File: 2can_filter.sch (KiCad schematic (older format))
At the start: 16 parts, among them J3 USB mini-B SMD, J4 NOT_FITTED_SWD_Conn_01x04_Male, U5 STM32F105RBTx, U6 TJA1040T, U7 TJA1040T, Y1 Crystal KX-13 25MHz

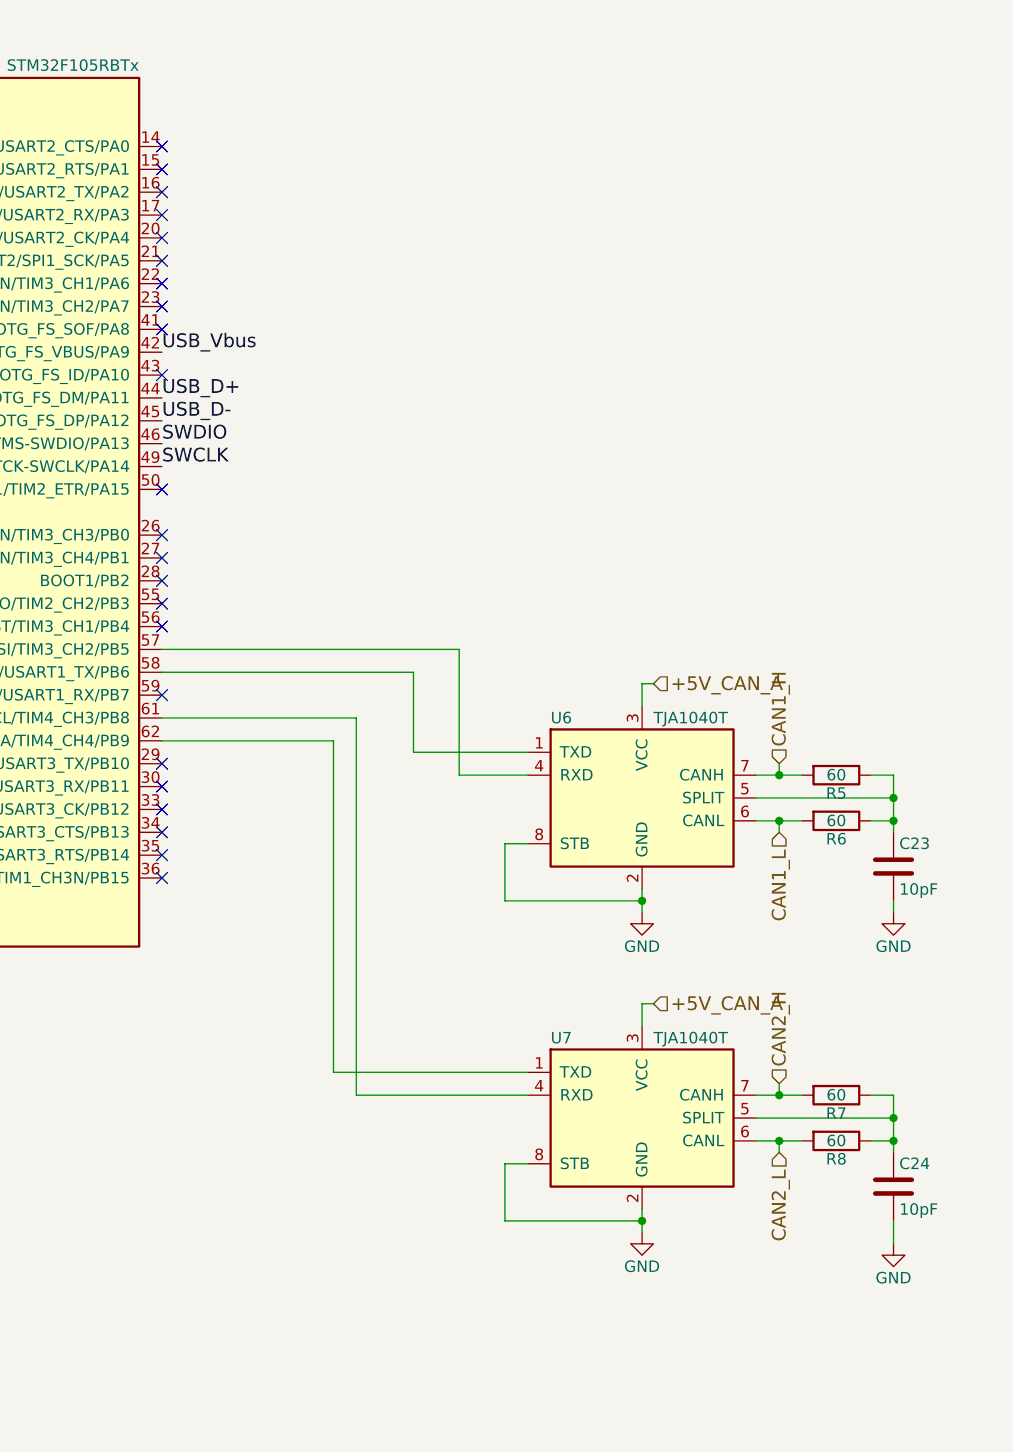
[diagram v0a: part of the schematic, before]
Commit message: add transient voltage suppression diods on CAN
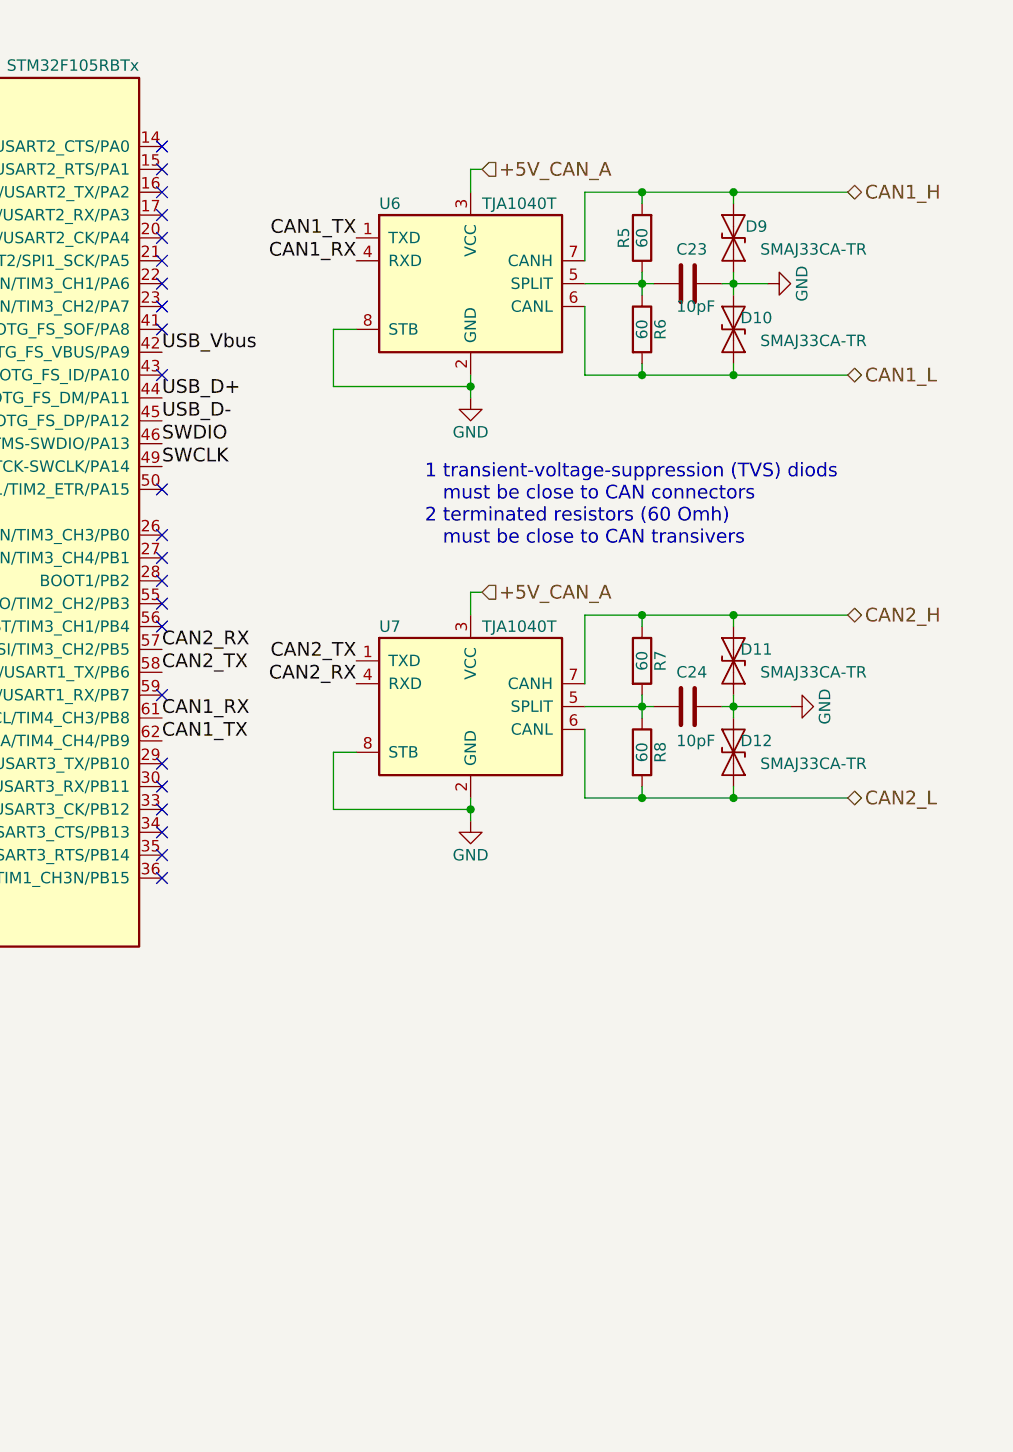
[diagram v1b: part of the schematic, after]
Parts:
- added D10, D11, D12, D9: SMAJ33CA-TR, Diodes_SMD:D_SMA, symbol D_TVS
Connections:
- net CAN1_H: now also D9.1 (A1)
- net CAN1_L: now also D10.2 (A2)
- net CAN2_H: now also R7.1, D11.1 (A1); no longer R7.2
- net CAN2_L: now also D12.2 (A2)
- net GND: now also C23.1, C24.1, D10.1 (A1), D11.2 (A2), D12.1 (A1), D9.2 (A2); no longer C23.2, C24.2
- net CAN1_TX: now reaches U5.62 (CAN1_TX/DAC_EXTI9/I2C1_SDA/TIM4_CH4/PB9)
- net CAN1_TX: now also U6.1 (TXD); no longer U7.1 (TXD)
- net CAN1_RX: now reaches U5.61 (CAN1_RX/I2C1_SCL/TIM4_CH3/PB8)
- net CAN1_RX: now also U6.4 (RXD); no longer U7.4 (RXD)
- net at R8.1, U7.5 (SPLIT): now also C24.2, R7.2; no longer C24.1, R7.1
- net CAN2_RX: now reaches U5.57 (CAN2_RX/I2C1_SMBA/I2S3_SD/SPI1_MOSI/SPI3_MOSI/TIM3_CH2/PB5)
- net CAN2_RX: now also U7.4 (RXD); no longer U6.4 (RXD)
- net CAN2_TX: now reaches U5.58 (CAN2_TX/I2C1_SCL/TIM4_CH1/USART1_TX/PB6)
- net CAN2_TX: now also U7.1 (TXD); no longer U6.1 (TXD)
- net at R5.1, R6.1, U6.5 (SPLIT): now also C23.2; no longer C23.1
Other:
- note added: "1 transient-voltage-suppression (TVS) diods\n must be close to CAN connectors\n2 terminated resistors (60 Omh)\n must be close to CAN transivers"
- moved on the sheet: C23, C24, R5, R6, R7, R8, U6, U7

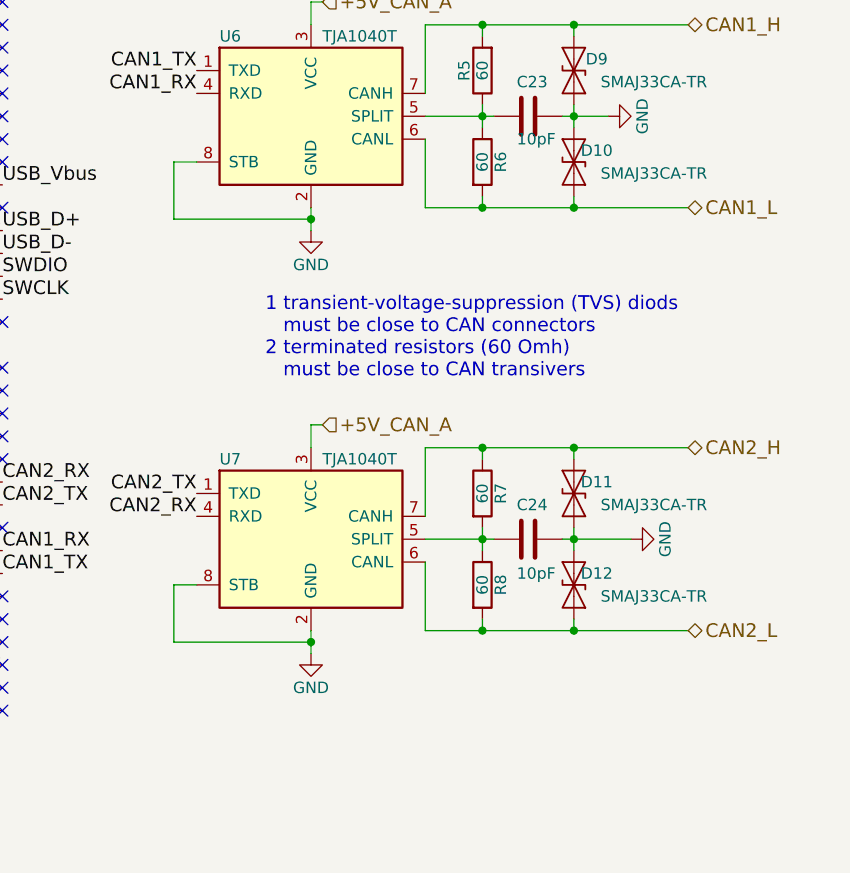
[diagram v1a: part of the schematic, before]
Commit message: add resistor on can STB pin module A
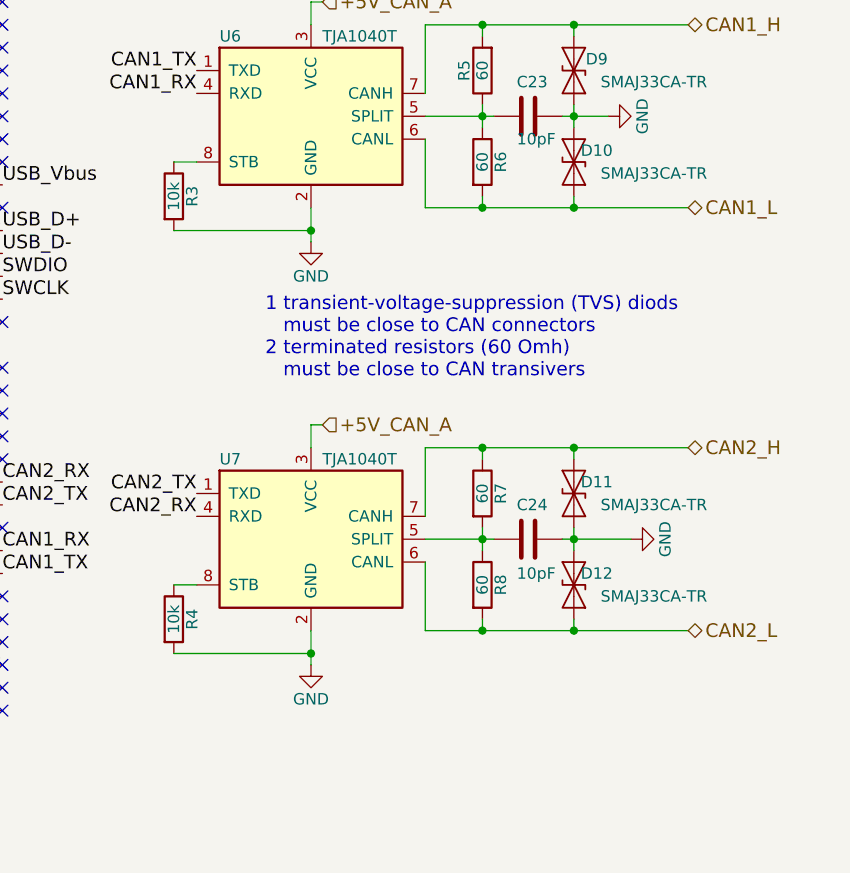
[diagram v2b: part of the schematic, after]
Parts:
- added R3, R4: 10k, Resistors_SMD:R_0805, symbol R
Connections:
- net GND: now also R3.2, R4.2; no longer U6.8 (STB), U7.8 (STB)
- new net: R4.1, U7.8 (STB)
- new net: R3.1, U6.8 (STB)
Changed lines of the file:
@@
 L GND #PWR08
 U 1 1 5A048D0B
-P 9050 2400
-F 0 "#PWR08" H 9050 2150 50  0001 C CNN
-F 1 "GND" H 9050 2250 50  0000 C CNN
-F 2 "" H 9050 2400 50  0001 C CNN
-F 3 "" H 9050 2400 50  0001 C CNN
-	1    9050 2400
+P 9050 2450
+F 0 "#PWR08" H 9050 2200 50  0001 C CNN
+F 1 "GND" H 9050 2300 50  0000 C CNN
+F 2 "" H 9050 2450 50  0001 C CNN
+F 3 "" H 9050 2450 50  0001 C CNN
+	1    9050 2450
 	1    0    0    -1
 $EndComp
@@
 L GND #PWR09
 U 1 1 5A09EB28
-P 9050 4250
-F 0 "#PWR09" H 9050 4000 50  0001 C CNN
-F 1 "GND" H 9050 4100 50  0000 C CNN
-F 2 "" H 9050 4250 50  0001 C CNN
-F 3 "" H 9050 4250 50  0001 C CNN
-	1    9050 4250
+P 9050 4300
+F 0 "#PWR09" H 9050 4050 50  0001 C CNN
+F 1 "GND" H 9050 4150 50  0000 C CNN
+F 2 "" H 9050 4300 50  0001 C CNN
+F 3 "" H 9050 4300 50  0001 C CNN
+	1    9050 4300
 	1    0    0    -1
 $EndComp
@@
 	9050 1500 9050 1400
 Wire Wire Line
-	8450 2100 8450 2350
-Wire Wire Line
 	8450 2100 8550 2100
 Wire Wire Line
-	9050 2300 9050 2400
+	9050 2300 9050 2450
 Wire Wire Line
 	8450 3950 8550 3950
 Wire Wire Line
-	9050 4150 9050 4250
+	9050 4150 9050 4300
 Wire Wire Line
 	2100 6800 2100 6650
@@
 Connection ~ 5600 6600
 Wire Wire Line
-	8450 2350 9050 2350
-Connection ~ 9050 2350
-Wire Wire Line
-	9050 4200 8450 4200
-Connection ~ 9050 4200
-Wire Wire Line
-	8450 4200 8450 3950
+	8450 2400 9050 2400
+Connection ~ 9050 2400
+Wire Wire Line
+	9050 4250 8450 4250
+Connection ~ 9050 4250
 Wire Wire Line
 	9050 3350 9050 3250
@@
 	9550 4150 10700 4150
 Wire Wire Line
-	10700 3350 9550 3350
+	9550 3350 10700 3350
 Wire Wire Line
 	9550 3350 9550 3650
@@
 Text Notes 8850 3050 0    60   ~ 0
 1 transient-voltage-suppression (TVS) diods\n   must be close to CAN connectors\n2 terminated resistors (60 Omh)\n   must be close to CAN transivers
+$Comp
+L R R3
+U 1 1 5A16A204
+P 8450 2250
+F 0 "R3" V 8530 2250 50  0000 C CNN
+F 1 "10k" V 8450 2250 50  0000 C CNN
+F 2 "Resistors_SMD:R_0805" V 8380 2250 50  0001 C CNN
+F 3 "" H 8450 2250 50  0001 C CNN
+	1    8450 2250
+	1    0    0    -1
+$EndComp
+$Comp
+L R R4
+U 1 1 5A16A369
+P 8450 4100
+F 0 "R4" V 8530 4100 50  0000 C CNN
+F 1 "10k" V 8450 4100 50  0000 C CNN
+F 2 "Resistors_SMD:R_0805" V 8380 4100 50  0001 C CNN
+F 3 "" H 8450 4100 50  0001 C CNN
+	1    8450 4100
+	1    0    0    -1
+$EndComp
 $EndSCHEMATC

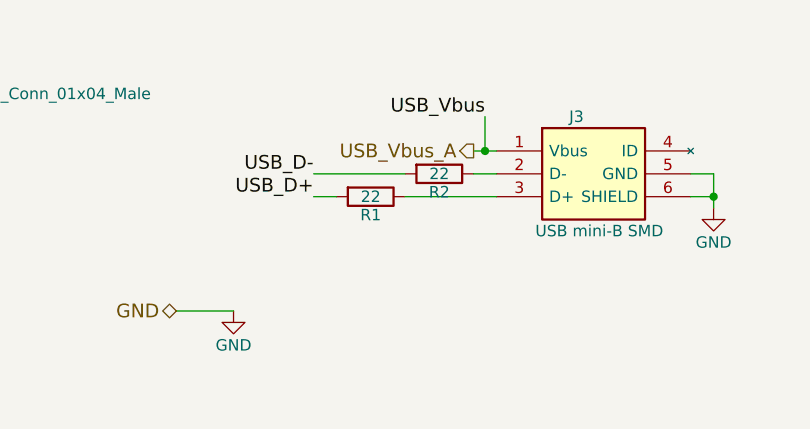
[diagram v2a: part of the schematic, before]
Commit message: fix signal trace length usb module A
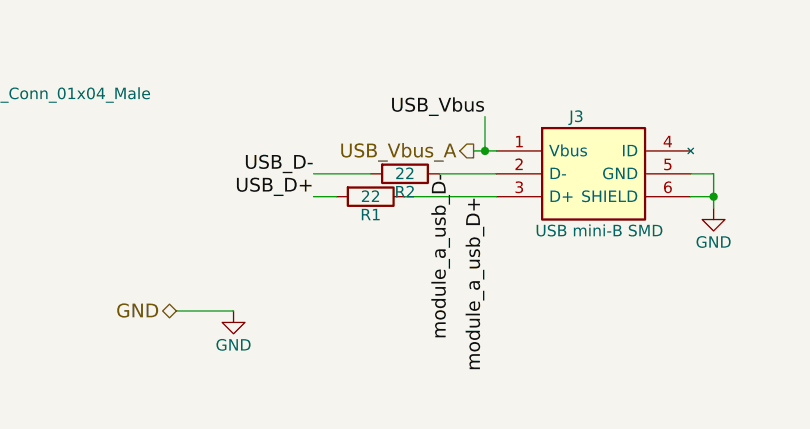
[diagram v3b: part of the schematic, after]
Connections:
- net module_a_usb_D-: now reaches J3.2 (D-), R2.1
- net module_a_usb_D+: now reaches J3.3 (D+), R1.1
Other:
- moved on the sheet: R2
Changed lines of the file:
@@
 L R R2
 U 1 1 5A0C2815
-P 4400 6500
-F 0 "R2" V 4480 6500 50  0000 C CNN
-F 1 "22" V 4400 6500 50  0000 C CNN
-F 2 "Resistors_SMD:R_0805" V 4330 6500 50  0001 C CNN
-F 3 "" H 4400 6500 50  0001 C CNN
-	1    4400 6500
+P 4250 6500
+F 0 "R2" V 4330 6500 50  0000 C CNN
+F 1 "22" V 4250 6500 50  0000 C CNN
+F 2 "Resistors_SMD:R_0805" V 4180 6500 50  0001 C CNN
+F 3 "" H 4250 6500 50  0001 C CNN
+	1    4250 6500
 	0    1    1    0
 $EndComp
@@
 	5600 6500 5600 6650
 Wire Wire Line
-	3850 6500 4250 6500
-Wire Wire Line
-	4550 6500 4650 6500
+	3850 6500 4100 6500
+Wire Wire Line
+	4400 6500 4650 6500
 Wire Wire Line
 	4650 6600 4250 6600
@@
 	1    0    0    -1
 $EndComp
+Text Label 4600 6600 3    60   ~ 0
+module_a_usb_D+
+Text Label 4450 6500 3    60   ~ 0
+module_a_usb_D-
 $EndSCHEMATC

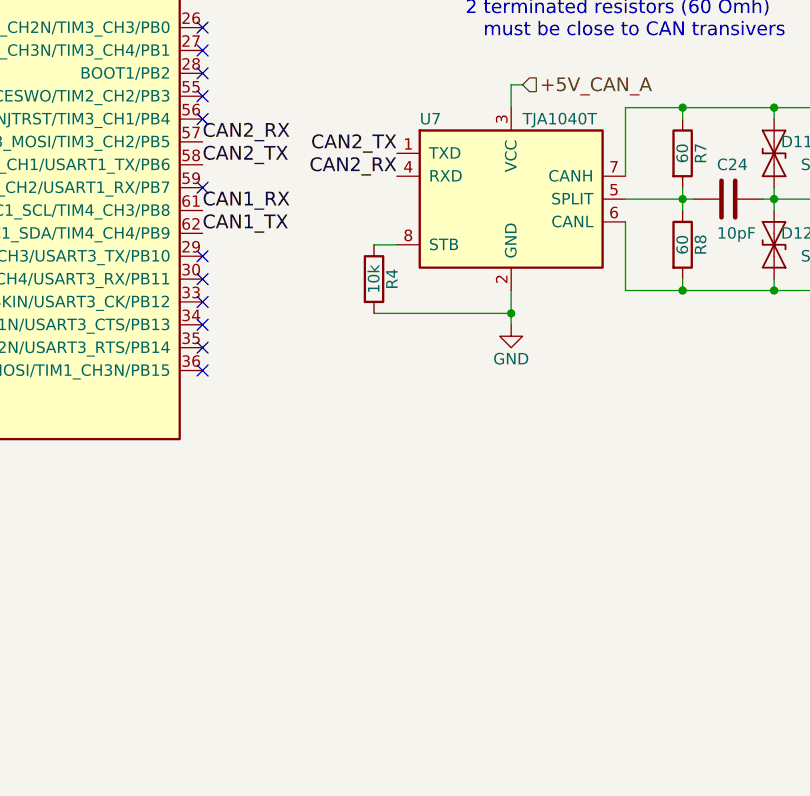
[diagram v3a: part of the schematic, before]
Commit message: sch&pcb: add LED`s and refresh readme image`s
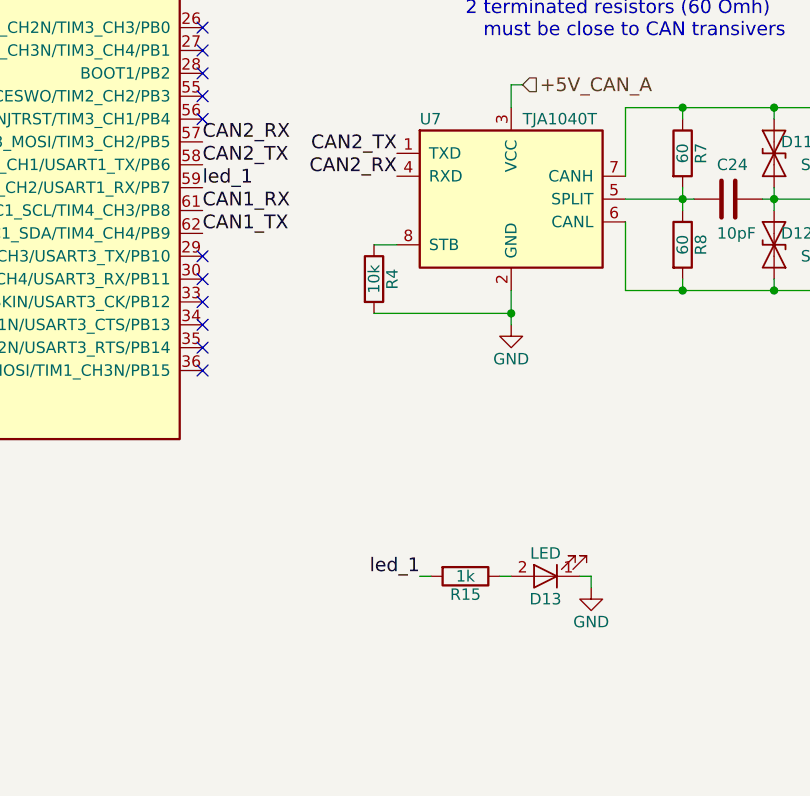
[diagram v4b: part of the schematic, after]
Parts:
- added D13: LED, LEDs:LED_0805, symbol LED
- added R15: 1k, Resistors_SMD:R_0805, symbol R
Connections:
- net GND: now also D13.1 (K)
- net led_1: now reaches U5.59 (I2C1_SDA/TIM4_CH2/USART1_RX/PB7)
- net led_1: now also R15.2
- new net: D13.2 (A), R15.1
- no-connect marks 42 -> 41
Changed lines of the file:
@@
 NoConn ~ 7700 4100
 NoConn ~ 7700 4000
-NoConn ~ 7700 3700
 NoConn ~ 7700 3400
 NoConn ~ 7700 3300
@@
 Text Label 4450 6500 3    60   ~ 0
 module_a_usb_D-
+$Comp
+L R R15
+U 1 1 5A2685DD
+P 8850 5400
+F 0 "R15" V 8930 5400 50  0000 C CNN
+F 1 "1k" V 8850 5400 50  0000 C CNN
+F 2 "Resistors_SMD:R_0805" V 8780 5400 50  0001 C CNN
+F 3 "" H 8850 5400 50  0001 C CNN
+	1    8850 5400
+	0    1    1    0
+$EndComp
+$Comp
+L LED D13
+U 1 1 5A26884C
+P 9200 5400
+F 0 "D13" H 9200 5500 50  0000 C CNN
+F 1 "LED" H 9200 5300 50  0000 C CNN
+F 2 "LEDs:LED_0805" H 9200 5400 50  0001 C CNN
+F 3 "" H 9200 5400 50  0001 C CNN
+	1    9200 5400
+	-1   0    0    1
+$EndComp
+Wire Wire Line
+	9000 5400 9050 5400
+Wire Wire Line
+	9350 5400 9400 5400
+Wire Wire Line
+	9400 5400 9400 5450
+Wire Wire Line
+	8700 5400 8650 5400
+$Comp
+L GND #PWR016
+U 1 1 5A268B13
+P 9400 5450
+F 0 "#PWR016" H 9400 5200 50  0001 C CNN
+F 1 "GND" H 9400 5300 50  0000 C CNN
+F 2 "" H 9400 5450 50  0001 C CNN
+F 3 "" H 9400 5450 50  0001 C CNN
+	1    9400 5450
+	1    0    0    -1
+$EndComp
+Text Label 8650 5400 2    60   ~ 0
+led_1
+Text Label 7700 3700 0    60   ~ 0
+led_1
 $EndSCHEMATC

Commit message: add usb 3d modele
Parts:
- J3: footprint zulljon:USB_mini_B -> zpkl:USB_mini_B
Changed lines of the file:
@@
 F 0 "J3" H 5000 6550 50  0000 C CNN
 F 1 "USB mini-B SMD" H 5100 6050 50  0000 C CNN
-F 2 "zulljon:USB_mini_B" H 5000 5950 50  0001 C CNN
+F 2 "zpkl:USB_mini_B" H 5000 5950 50  0001 C CNN
 F 3 "http://www.molex.com/webdocs/datasheets/pdf/en-us/0548190572_IO_CONNECTORS.pdf" H 5000 5850 50  0001 C CNN
 F 4 "Surface mount onthego connector,1A 30V Molex On-The-Go Series Right Angle SMT Version 2.0 Type B Mini USB Connector Receptacle, 30 V, 1A" H 5000 5750 50  0001 C CNN "Description"

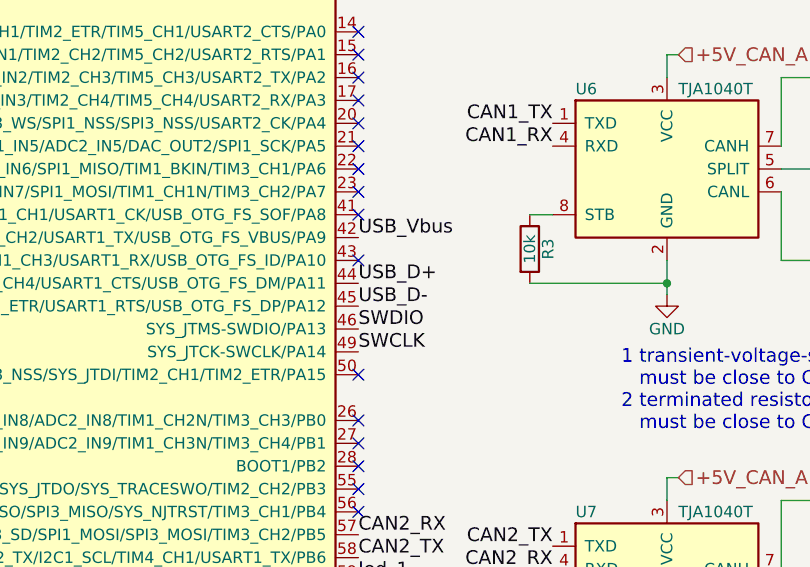
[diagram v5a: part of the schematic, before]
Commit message: fix USB, swapped the traces D+ D-
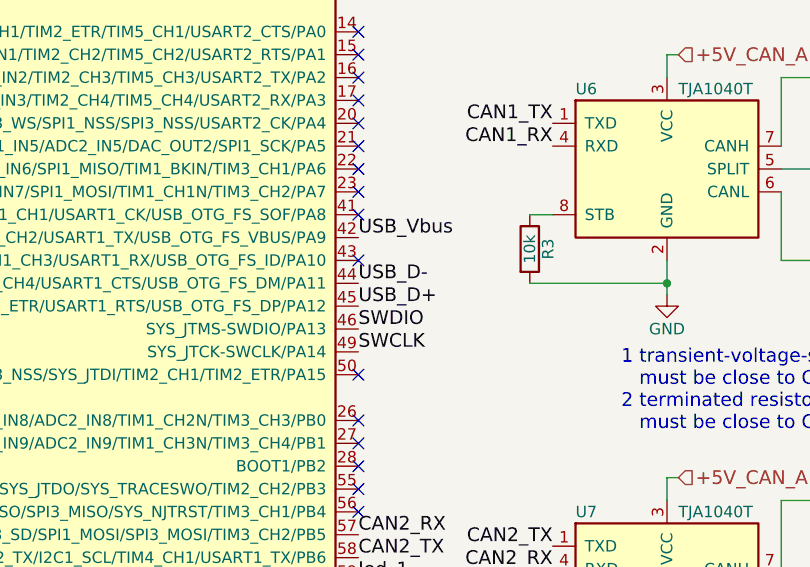
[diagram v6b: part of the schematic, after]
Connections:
- net USB_D+: now also U5.45 (CAN1_TX/TIM1_ETR/USART1_RTS/USB_OTG_FS_DP/PA12); no longer U5.44 (ADC1_EXTI11/ADC2_EXTI11/CAN1_RX/TIM1_CH4/USART1_CTS/USB_OTG_FS_DM/PA11)
- net USB_D-: now also U5.44 (ADC1_EXTI11/ADC2_EXTI11/CAN1_RX/TIM1_CH4/USART1_CTS/USB_OTG_FS_DM/PA11); no longer U5.45 (CAN1_TX/TIM1_ETR/USART1_RTS/USB_OTG_FS_DP/PA12)
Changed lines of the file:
@@
 Text Label 3850 6500 2    60   ~ 0
 USB_D-
+Text Label 7700 2500 0    60   ~ 0
+USB_D+
 Text Label 7700 2400 0    60   ~ 0
-USB_D+
-Text Label 7700 2500 0    60   ~ 0
 USB_D-
 Text Label 7700 2200 0    60   ~ 0
